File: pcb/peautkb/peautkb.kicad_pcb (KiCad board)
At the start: 4 copper layers, 3.6 x 3.1 mm, 184 parts, among them J1 Conn_01x04, J2 MJ-4PP-9, J3 Conn_01x04, J4 MJ-4PP-9, SW1 SW_PUSH, SW10 SW_PUSH, SW11 SW_PUSH, SW12 SW_PUSH, SW13 SW_PUSH, SW14 SW_PUSH, SW15 SW_PUSH, SW16 SW_PUSH, SW17 SW_PUSH, SW18 SW_PUSH, SW19 SW_PUSH, SW2 SW_PUSH, SW20 SW_PUSH, SW21 SW_PUSH, SW22 SW_PUSH, SW23 SW_PUSH, SW24 SW_PUSH, SW25 SW_PUSH, SW26 SW_PUSH, SW27 SW_PUSH, SW28 Rotary_Encoder_Switch, SW29 SW_PUSH, SW3 SW_PUSH, SW30 SW_PUSH, SW31 SW_PUSH, SW32 SW_PUSH, SW33 SW_PUSH, SW34 SW_PUSH, SW35 SW_PUSH, SW36 SW_PUSH, SW37 SW_PUSH, SW38 SW_PUSH, SW39 SW_PUSH, SW4 SW_PUSH, SW40 SW_PUSH, SW41 SW_PUSH, SW42 SW_PUSH, SW43 SW_PUSH, SW44 SW_PUSH, SW45 SW_PUSH, SW46 SW_PUSH, SW47 SW_PUSH, SW48 SW_PUSH, SW49 SW_PUSH, SW5 SW_PUSH, SW50 SW_PUSH, SW51 SW_PUSH, SW52 SW_PUSH, SW53 SW_PUSH, SW54 SW_PUSH, SW55 SW_PUSH, SW56 SW_PUSH, SW57 Rotary_Encoder_Switch, SW58 SW_PUSH, SW6 SW_PUSH, SW7 SW_PUSH, SW8 SW_PUSH, SW9 SW_PUSH, U1 black-pill-v3, U2 black-pill-v3

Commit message: left side traces completed
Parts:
- removed D2, D3, D36, D37, D38, D4: D, kbd:D3_SMD_v2
- removed SW1, SW2, SW3, SW30, SW31, SW32: SW_PUSH, kbd:CherryMX_Hotswap
- added REF**: Breakaway_Tabs, kbd:Breakaway_Tabs, F.Cu at (17.8, 89.2)
- added REF**: Breakaway_Tabs, kbd:Breakaway_Tabs, F.Cu at (182.0, 80.4)
- added REF**: Breakaway_Tabs, kbd:Breakaway_Tabs, F.Cu at (189.8, 37.2)
- added REF**: Breakaway_Tabs, kbd:Breakaway_Tabs, F.Cu at (182.0, 37.3)
- added REF**: Breakaway_Tabs, kbd:Breakaway_Tabs, F.Cu at (189.7, 80.4)
- added REF**: Breakaway_Tabs, kbd:Breakaway_Tabs, F.Cu at (353.9, 44.9)
- added REF**: Breakaway_Tabs, kbd:Breakaway_Tabs, F.Cu at (353.8, 88.8)
- added REF**: Breakaway_Tabs, kbd:Breakaway_Tabs, F.Cu at (344.2, 97.7)
- added REF**: Breakaway_Tabs, kbd:Breakaway_Tabs, F.Cu at (292.5, 97.7)
- added REF**: Breakaway_Tabs, kbd:Breakaway_Tabs, F.Cu at (17.8, 46.8)
- added REF**: Breakaway_Tabs, kbd:Breakaway_Tabs, F.Cu at (28.3, 97.7)
- added REF**: Breakaway_Tabs, kbd:Breakaway_Tabs, F.Cu at (79.3, 97.7)
- D1, D10, D11, D12, D13, D14, D15, D16, D17, D18, D19, D20, D21, D22, D23, D24, D25, D26, D27, D28, D29, D30, D31, D32, D33, D35, D39, D40, D41, D42, D43, D44, D45, D46, D47, D48, D49, D5, D50, D51, D56, D6, D61, D62, D7, D8, D9, LED1, LED10, LED11, LED12, LED13, LED14, LED15, LED16, LED17, LED18, LED19, LED2, LED20, LED21, LED22, LED23, LED24, LED25, LED26, LED27, LED28, LED29, LED3, LED30, LED31, LED32, LED33, LED34, LED35, LED36, LED37, LED38, LED39, LED4, LED40, LED41, LED42, LED43, LED44, LED45, LED46, LED47, LED48, LED49, LED5, LED50, LED6, LED7, LED8, LED9: moved to B.Cu
- D52, D53, D54, D55, D57, D58, D59, D60, D63, D64, D65, D66, D67, D68, D69, D70: footprint kbd:D3_SMD -> kbd:D3_SMD_v2; moved to B.Cu
- moved LED3 340.6 mm to (27.4, 92.4), turned to 180 degrees
- moved SW4 303.1 mm to (27.4, 50.0)
- moved LED2 299.6 mm to (27.5, 73.5)
- moved SW58 288.1 mm to (210.7, 106.2), turned to 26.7 degrees
- moved SW5 286.9 mm to (27.4, 69.0)
- moved SW42 286.4 mm to (306.2, 69.0)
- moved SW37 282.9 mm to (325.2, 63.3)
- moved SW38 281.8 mm to (325.2, 82.3)
- moved SW35 279.6 mm to (344.1, 88.0)
- moved SW6 271.2 mm to (27.4, 88.0)
- moved D10 266.3 mm to (54.7, 43.4), turned to 90 degrees
- moved LED50 266.1 mm to (212.8, 110.0), turned to 26.7 degrees
- moved SW41 265.3 mm to (287.2, 88.0)
- moved SW45 265.0 mm to (267.4, 89.2), turned to 6.7 degrees
- moved SW53 263.4 mm to (228.9, 98.3), turned to 20 degrees
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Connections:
- D18 pad 2: Net-(D13-Pad4) -> LLED_In
- D22 pad 2: Net-(D18-Pad4) -> Net-(D22-Pad2)
- D46 pad 2: Net-(D42-Pad4) -> RLED_In
- D5 pad 2: Net-(D1-Pad4) -> Net-(D5-Pad2)
- D51 pad 2: Net-(D46-Pad4) -> Net-(D51-Pad2)
- D56 pad 2: Net-(D51-Pad4) -> Net-(D56-Pad2)
- D61 pad 2: Net-(D56-Pad4) -> Net-(D61-Pad2)
- D62 pad 2: Net-(D61-Pad4) -> Net-(D62-Pad2)
- D9 pad 2: Net-(D5-Pad4) -> Net-(D9-Pad2)
- D9 pad 4: Net-(D13-Pad2) -> Net-(D9-Pad4)
- LED11 pad 4: Net-(LED11-Pad4) -> Net-(D9-Pad4)
- LED12 pad 2: Net-(LED11-Pad4) -> Net-(LED12-Pad2)
- LED13 pad 2: Net-(LED12-Pad4) -> Net-(LED13-Pad2)
- LED13 pad 4: Net-(LED13-Pad4) -> Net-(D13-Pad4)
- LED14 pad 2: Net-(LED13-Pad4) -> Net-(LED14-Pad2)
- LED14 pad 4: Net-(LED14-Pad4) -> Net-(LED10-Pad2)
- LED15 pad 2: Net-(LED15-Pad2) -> Net-(D9-Pad2)
- LED16 pad 4: Net-(LED15-Pad2) -> Net-(LED12-Pad2)
- LED17 pad 2: Net-(LED17-Pad2) -> Net-(D13-Pad2)
- LED17 pad 4: Net-(LED16-Pad2) -> Net-(LED17-Pad4)
- LED18 pad 2: Net-(LED14-Pad4) -> Net-(LED18-Pad2)
- LED18 pad 4: Net-(LED17-Pad2) -> Net-(LED14-Pad2)
- LED20 pad 2: Net-(LED19-Pad4) -> Net-(LED20-Pad2)
- LED20 pad 4: Net-(LED20-Pad4) -> Net-(LED16-Pad2)
- LED21 pad 2: Net-(LED20-Pad4) -> Net-(LED17-Pad4)
- LED22 pad 2: Net-(LED21-Pad4) -> Net-(LED22-Pad2)
- LED22 pad 4: Net-(LED22-Pad4) -> Net-(LED18-Pad2)
- LED23 pad 2: Net-(LED23-Pad2) -> Net-(LED19-Pad4)
- LED23 pad 4: LLED_In -> Net-(D18-Pad4)
- LED24 pad 2: Net-(LED24-Pad2) -> Net-(LED21-Pad4)
- LED24 pad 4: Net-(LED23-Pad2) -> Net-(LED20-Pad2)
- LED25 pad 2: Net-(LED22-Pad4) -> Net-(D22-Pad2)
- LED25 pad 4: Net-(LED24-Pad2) -> Net-(LED22-Pad2)
- LED28 pad 2: Net-(D42-Pad2) -> Net-(LED28-Pad2)
- LED28 pad 4: Net-(LED27-Pad2) -> Net-(LED28-Pad4)
- LED29 pad 4: Net-(LED29-Pad4) -> Net-(D51-Pad4)
- LED3 pad 2: Net-(D1-Pad2) -> Net-(LED10-Pad4)
- LED3 pad 4: Net-(LED2-Pad2) -> Net-(LED3-Pad4)
- LED30 pad 2: Net-(LED29-Pad4) -> Net-(LED30-Pad2)
- LED30 pad 4: Net-(LED30-Pad4) -> Net-(LED27-Pad2)
- LED31 pad 2: Net-(LED30-Pad4) -> Net-(LED28-Pad4)
- LED31 pad 4: Net-(LED31-Pad4) -> Net-(D56-Pad4)
- LED32 pad 2: Net-(LED32-Pad2) -> Net-(D51-Pad2)
- LED33 pad 4: Net-(LED32-Pad2) -> Net-(LED30-Pad2)
- LED34 pad 2: Net-(LED34-Pad2) -> Net-(D56-Pad2)
- LED34 pad 4: Net-(LED33-Pad2) -> Net-(LED34-Pad4)
- LED35 pad 2: Net-(LED31-Pad4) -> Net-(LED35-Pad2)
- LED35 pad 4: Net-(LED34-Pad2) -> Net-(LED28-Pad2)
- LED36 pad 4: Net-(LED36-Pad4) -> Net-(D42-Pad4)
- LED37 pad 2: Net-(LED36-Pad4) -> Net-(LED37-Pad2)
- LED37 pad 4: Net-(LED37-Pad4) -> Net-(LED33-Pad2)
- LED38 pad 2: Net-(LED37-Pad4) -> Net-(LED34-Pad4)
- LED38 pad 4: Net-(LED38-Pad4) -> Net-(D61-Pad4)
- LED39 pad 2: Net-(LED38-Pad4) -> Net-(LED39-Pad2)
- LED39 pad 4: Net-(LED39-Pad4) -> Net-(LED35-Pad2)
- LED4 pad 4: Net-(LED4-Pad4) -> Net-(D1-Pad4)
- LED40 pad 2: Net-(LED40-Pad2) -> Net-(D42-Pad2)
- LED41 pad 4: Net-(LED40-Pad2) -> Net-(LED37-Pad2)
- LED42 pad 2: Net-(LED42-Pad2) -> Net-(D61-Pad2)
- LED42 pad 4: Net-(LED41-Pad2) -> Net-(LED42-Pad4)
- LED43 pad 2: Net-(LED39-Pad4) -> Net-(LED43-Pad2)
- LED43 pad 4: Net-(LED42-Pad2) -> Net-(LED39-Pad2)
- LED45 pad 2: Net-(LED44-Pad4) -> Net-(LED45-Pad2)
- LED45 pad 4: Net-(LED45-Pad4) -> Net-(LED41-Pad2)
- LED46 pad 2: Net-(LED45-Pad4) -> Net-(LED42-Pad4)
- LED47 pad 2: Net-(LED46-Pad4) -> Net-(LED47-Pad2)
- LED47 pad 4: Net-(LED47-Pad4) -> Net-(LED43-Pad2)
- LED48 pad 2: Net-(LED48-Pad2) -> Net-(LED44-Pad4)
- LED48 pad 4: RLED_In -> Net-(D46-Pad4)
- LED49 pad 2: Net-(LED49-Pad2) -> Net-(LED46-Pad4)
- LED49 pad 4: Net-(LED48-Pad2) -> Net-(LED45-Pad2)
- LED5 pad 2: Net-(LED4-Pad4) -> Net-(LED5-Pad2)
- LED5 pad 4: Net-(LED5-Pad4) -> Net-(LED2-Pad2)
- LED50 pad 2: Net-(LED47-Pad4) -> Net-(D62-Pad2)
- LED50 pad 4: Net-(LED49-Pad2) -> Net-(LED47-Pad2)
- LED6 pad 2: Net-(LED5-Pad4) -> Net-(LED3-Pad4)
- LED6 pad 4: Net-(LED10-Pad2) -> Net-(D5-Pad4)
- LED7 pad 2: Net-(LED7-Pad2) -> Net-(D1-Pad2)
- LED8 pad 2: Net-(LED8-Pad2) -> Net-(LED12-Pad4)
- LED8 pad 4: Net-(LED7-Pad2) -> Net-(LED5-Pad2)
- LED9 pad 2: Net-(LED10-Pad4) -> Net-(D5-Pad2)
- LED9 pad 4: Net-(LED8-Pad2) -> Net-(LED13-Pad2)
- SW8 pad 1: Net-(SW8-Pad1) -> LCol2
- SW9 pad 1: Net-(SW8-Pad1) -> LCol2
- U1 pad 33: LCol0 -> Net-(U1-Pad33)
- U1 pad 34: LRow0 -> LRow3
- U1 pad 35: LRow1 -> LRow2
- U1 pad 36: LRow2 -> LRow1
- U1 pad 37: LRow3 -> LRow0
- U2 pad 33: RCol0 -> Net-(U2-Pad33)
- U2 pad 34: RRow0 -> RRow3
- U2 pad 35: RRow1 -> RRow2
- U2 pad 36: RRow2 -> RRow1
- U2 pad 37: RRow3 -> RRow0
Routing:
- net LCol1: track 0.00 -> 230.7 mm
- net LCol3: track 0.00 -> 228.8 mm, vias 0 -> 7
- net LCol2: track 0.00 -> 218.8 mm, vias 0 -> 6
- net LCol4: track 0.00 -> 218.1 mm, vias 0 -> 7
- net LCol5: track 0.00 -> 196.7 mm, vias 0 -> 7
- net LRow1: track 0.00 -> 194.5 mm, vias 0 -> 2
- net LRow2: track 0.00 -> 192.3 mm, vias 0 -> 6
- net LRow3: track 0.00 -> 184.7 mm, vias 0 -> 7
- net LCol6: track 0.00 -> 182.3 mm, vias 0 -> 7
- net LRow0: track 0.00 -> 180.0 mm
- net LCol7: track 0.00 -> 166.9 mm, vias 0 -> 4
- net GND1: track 0.00 -> 60.9 mm, vias 0 -> 31
- net Net-(LED10-Pad4): track 0.00 -> 58.6 mm
- net LUSART_RX: track 0.00 -> 57.8 mm, vias 0 -> 1
- net LUSART_TX: track 0.00 -> 55.1 mm
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- added copper zone on In1.Cu, net GND1
- added copper zone on In2.Cu, net VDD
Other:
- board size 3.6 x 3.1 mm -> 348 x 113 mm

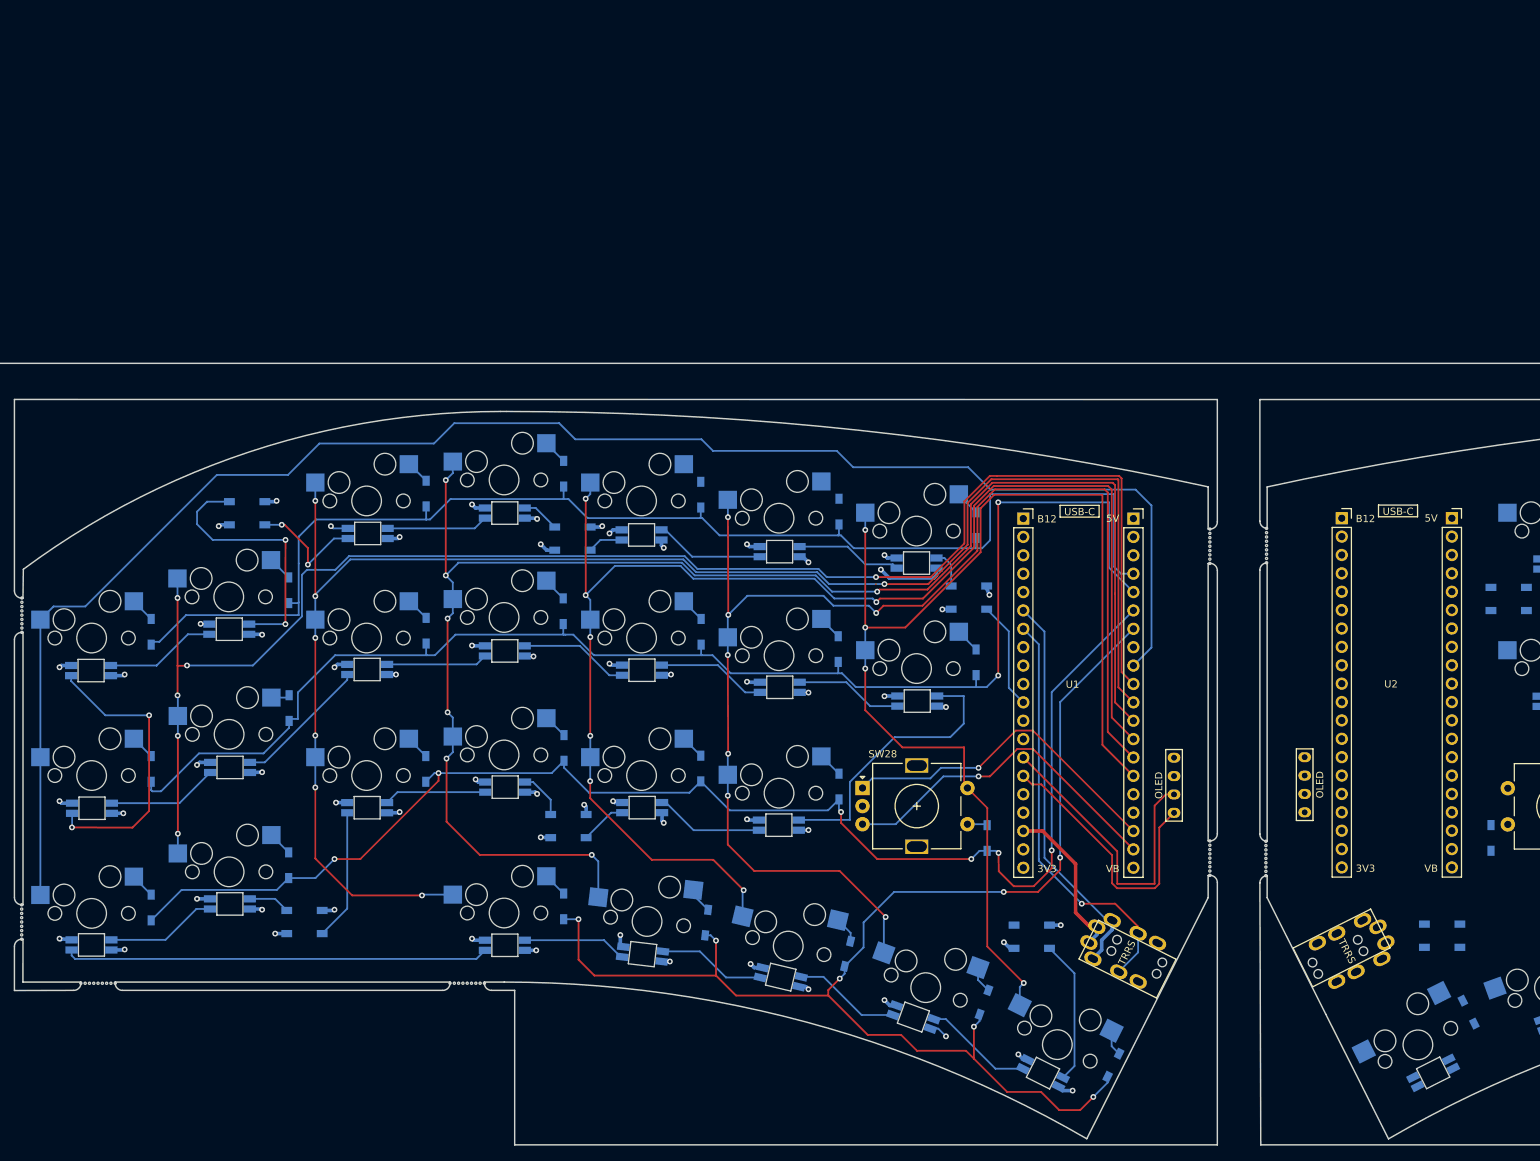
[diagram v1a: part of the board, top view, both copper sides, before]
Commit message: aadded decoup caps to LHS
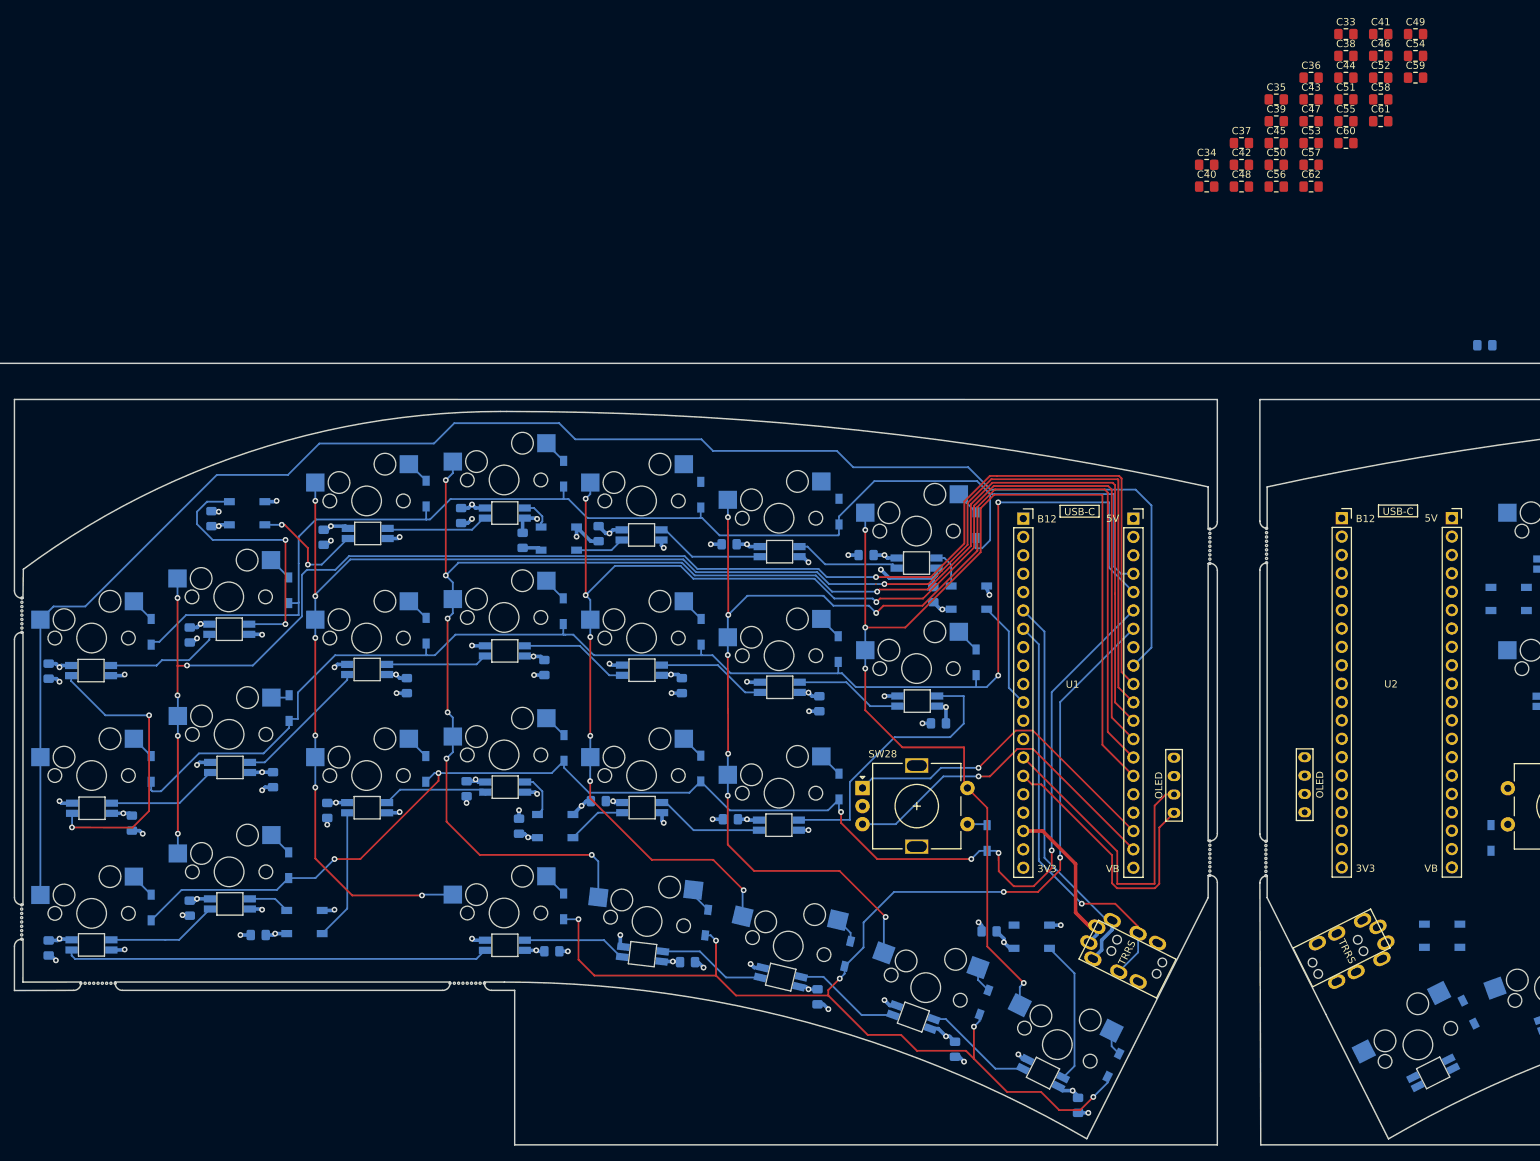
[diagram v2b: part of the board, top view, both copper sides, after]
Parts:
- added C1: 100nF, Capacitor_SMD:C_0805_2012Metric_Pad1.18x1.45mm_HandSolder, B.Cu at (79.2, 70.8)
- added C10: 100nF, Capacitor_SMD:C_0805_2012Metric_Pad1.18x1.45mm_HandSolder, B.Cu at (87.0, 36.5)
- added C11: 100nF, Capacitor_SMD:C_0805_2012Metric_Pad1.18x1.45mm_HandSolder, B.Cu at (127.8, 99.5)
- added C12: 100nF, Capacitor_SMD:C_0805_2012Metric_Pad1.18x1.45mm_HandSolder, B.Cu at (52.5, 69.5)
- added C13: 100nF, Capacitor_SMD:C_0805_2012Metric_Pad1.18x1.45mm_HandSolder, B.Cu at (115.7, 75.0)
- added C14: 100nF, Capacitor_SMD:C_0805_2012Metric_Pad1.18x1.45mm_HandSolder, B.Cu at (97.5, 35.5)
- added C15: 100nF, Capacitor_SMD:C_0805_2012Metric_Pad1.18x1.45mm_HandSolder, B.Cu at (50.5, 91.0)
- added C16: 100nF, Capacitor_SMD:C_0805_2012Metric_Pad1.18x1.45mm_HandSolder, B.Cu at (44.0, 33.5)
- added C17: 100nF, Capacitor_SMD:C_0805_2012Metric_Pad1.18x1.45mm_HandSolder, B.Cu at (163.8, 114.5)
- added C18: 100nF, Capacitor_SMD:C_0805_2012Metric_Pad1.18x1.45mm_HandSolder, B.Cu at (115.5, 37.0)
- added C19: 100nF, Capacitor_SMD:C_0805_2012Metric_Pad1.18x1.45mm_HandSolder, B.Cu at (90.0, 54.0)
- added C2: 100nF, Capacitor_SMD:C_0805_2012Metric_Pad1.18x1.45mm_HandSolder, B.Cu at (144.5, 61.8)
- added C20: 100nF, Capacitor_SMD:C_0805_2012Metric_Pad1.18x1.45mm_HandSolder, B.Cu at (60.0, 73.8)
- added C21: 100nF, Capacitor_SMD:C_0805_2012Metric_Pad1.18x1.45mm_HandSolder, B.Cu at (59.5, 36.0)
- added C22: 100nF, Capacitor_SMD:C_0805_2012Metric_Pad1.18x1.45mm_HandSolder, B.Cu at (146.8, 106.8)
- added C23: 100nF, Capacitor_SMD:C_0805_2012Metric_Pad1.18x1.45mm_HandSolder, B.Cu at (33.0, 75.5)
- added C24: 100nF, Capacitor_SMD:C_0805_2012Metric_Pad1.18x1.45mm_HandSolder, B.Cu at (134.5, 38.5)
- added C25: 100nF, Capacitor_SMD:C_0805_2012Metric_Pad1.18x1.45mm_HandSolder, B.Cu at (151.5, 90.5)
- added C26: 100nF, Capacitor_SMD:C_0805_2012Metric_Pad1.18x1.45mm_HandSolder, B.Cu at (78.5, 33.0)
- added C27: 100nF, Capacitor_SMD:C_0805_2012Metric_Pad1.18x1.45mm_HandSolder, B.Cu at (97.5, 72.5)
- added C28: 100nF, Capacitor_SMD:C_0805_2012Metric_Pad1.18x1.45mm_HandSolder, B.Cu at (109.8, 94.8)
- added C29: 100nF, Capacitor_SMD:C_0805_2012Metric_Pad1.18x1.45mm_HandSolder, B.Cu at (21.5, 54.5)
- added C3: 100nF, Capacitor_SMD:C_0805_2012Metric_Pad1.18x1.45mm_HandSolder, B.Cu at (41.0, 87.3)
- added C30: 100nF, Capacitor_SMD:C_0805_2012Metric_Pad1.18x1.45mm_HandSolder, B.Cu at (143.8, 44.0)
- added C31: 100nF, Capacitor_SMD:C_0805_2012Metric_Pad1.18x1.45mm_HandSolder, B.Cu at (109.0, 56.5)
- added C32: 100nF, Capacitor_SMD:C_0805_2012Metric_Pad1.18x1.45mm_HandSolder, B.Cu at (220.0, 9.50)
- added C33: 100nF, Capacitor_SMD:C_0805_2012Metric_Pad1.18x1.45mm_HandSolder, F.Cu at (200.8, -33.5)
- added C34: 100nF, Capacitor_SMD:C_0805_2012Metric_Pad1.18x1.45mm_HandSolder, F.Cu at (181.5, -15.4)
- added C35: 100nF, Capacitor_SMD:C_0805_2012Metric_Pad1.18x1.45mm_HandSolder, F.Cu at (191.1, -24.5)
- added C36: 100nF, Capacitor_SMD:C_0805_2012Metric_Pad1.18x1.45mm_HandSolder, F.Cu at (196.0, -27.5)
- added C37: 100nF, Capacitor_SMD:C_0805_2012Metric_Pad1.18x1.45mm_HandSolder, F.Cu at (186.3, -18.4)
- added C38: 100nF, Capacitor_SMD:C_0805_2012Metric_Pad1.18x1.45mm_HandSolder, F.Cu at (200.8, -30.5)
- added C39: 100nF, Capacitor_SMD:C_0805_2012Metric_Pad1.18x1.45mm_HandSolder, F.Cu at (191.1, -21.5)
- added C4: 100nF, Capacitor_SMD:C_0805_2012Metric_Pad1.18x1.45mm_HandSolder, B.Cu at (71.0, 56.5)
- added C40: 100nF, Capacitor_SMD:C_0805_2012Metric_Pad1.18x1.45mm_HandSolder, F.Cu at (181.5, -12.4)
- added C41: 100nF, Capacitor_SMD:C_0805_2012Metric_Pad1.18x1.45mm_HandSolder, F.Cu at (205.6, -33.5)
- added C42: 100nF, Capacitor_SMD:C_0805_2012Metric_Pad1.18x1.45mm_HandSolder, F.Cu at (186.3, -15.4)
- added C43: 100nF, Capacitor_SMD:C_0805_2012Metric_Pad1.18x1.45mm_HandSolder, F.Cu at (196.0, -24.5)
- added C44: 100nF, Capacitor_SMD:C_0805_2012Metric_Pad1.18x1.45mm_HandSolder, F.Cu at (200.8, -27.5)
- added C45: 100nF, Capacitor_SMD:C_0805_2012Metric_Pad1.18x1.45mm_HandSolder, F.Cu at (191.1, -18.4)
- added C46: 100nF, Capacitor_SMD:C_0805_2012Metric_Pad1.18x1.45mm_HandSolder, F.Cu at (205.6, -30.5)
- added C47: 100nF, Capacitor_SMD:C_0805_2012Metric_Pad1.18x1.45mm_HandSolder, F.Cu at (196.0, -21.5)
- added C48: 100nF, Capacitor_SMD:C_0805_2012Metric_Pad1.18x1.45mm_HandSolder, F.Cu at (186.3, -12.4)
- added C49: 100nF, Capacitor_SMD:C_0805_2012Metric_Pad1.18x1.45mm_HandSolder, F.Cu at (210.4, -33.5)
- added C5: 100nF, Capacitor_SMD:C_0805_2012Metric_Pad1.18x1.45mm_HandSolder, B.Cu at (86.5, 76.0)
- added C50: 100nF, Capacitor_SMD:C_0805_2012Metric_Pad1.18x1.45mm_HandSolder, F.Cu at (191.1, -15.4)
- added C51: 100nF, Capacitor_SMD:C_0805_2012Metric_Pad1.18x1.45mm_HandSolder, F.Cu at (200.8, -24.5)
- added C52: 100nF, Capacitor_SMD:C_0805_2012Metric_Pad1.18x1.45mm_HandSolder, F.Cu at (205.6, -27.5)
- added C53: 100nF, Capacitor_SMD:C_0805_2012Metric_Pad1.18x1.45mm_HandSolder, F.Cu at (196.0, -18.4)
- added C54: 100nF, Capacitor_SMD:C_0805_2012Metric_Pad1.18x1.45mm_HandSolder, F.Cu at (210.4, -30.5)
- added C55: 100nF, Capacitor_SMD:C_0805_2012Metric_Pad1.18x1.45mm_HandSolder, F.Cu at (200.8, -21.5)
- added C56: 100nF, Capacitor_SMD:C_0805_2012Metric_Pad1.18x1.45mm_HandSolder, F.Cu at (191.1, -12.4)
- added C57: 100nF, Capacitor_SMD:C_0805_2012Metric_Pad1.18x1.45mm_HandSolder, F.Cu at (196.0, -15.4)
- added C58: 100nF, Capacitor_SMD:C_0805_2012Metric_Pad1.18x1.45mm_HandSolder, F.Cu at (205.6, -24.5)
- added C59: 100nF, Capacitor_SMD:C_0805_2012Metric_Pad1.18x1.45mm_HandSolder, F.Cu at (210.4, -27.5)
- added C6: 100nF, Capacitor_SMD:C_0805_2012Metric_Pad1.18x1.45mm_HandSolder, B.Cu at (91.0, 93.2)
- added C60: 100nF, Capacitor_SMD:C_0805_2012Metric_Pad1.18x1.45mm_HandSolder, F.Cu at (200.8, -18.4)
- added C61: 100nF, Capacitor_SMD:C_0805_2012Metric_Pad1.18x1.45mm_HandSolder, F.Cu at (205.6, -21.5)
- added C62: 100nF, Capacitor_SMD:C_0805_2012Metric_Pad1.18x1.45mm_HandSolder, F.Cu at (196.0, -12.4)
- added C7: 100nF, Capacitor_SMD:C_0805_2012Metric_Pad1.18x1.45mm_HandSolder, B.Cu at (41.0, 49.5)
- added C8: 100nF, Capacitor_SMD:C_0805_2012Metric_Pad1.18x1.45mm_HandSolder, B.Cu at (128.0, 59.0)
- added C9: 100nF, Capacitor_SMD:C_0805_2012Metric_Pad1.18x1.45mm_HandSolder, B.Cu at (21.5, 92.8)
- moved D9 1.88 mm to (92.0, 36.2)
- moved D13 1.82 mm to (91.5, 75.9)
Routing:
- net GND1: track 60.9 -> 106.8 mm, vias 31 -> 58
- net VDD: track 52.3 -> 96.4 mm, vias 31 -> 30
- net LRow0: track 180.0 -> 185.0 mm
- net Net-(D9-Pad2): track 4.93 -> 6.82 mm
- net Net-(D13-Pad2): track 6.42 -> 8.25 mm
- net Net-(D9-Pad4): track 5.24 -> 4.46 mm
- net Net-(LED13-Pad2): track 14.2 -> 14.9 mm

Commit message: finished RHS
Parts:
- C33, C34, C35, C36, C37, C38, C39, C40, C41, C42, C43, C44, C45, C46, C47, C48, C49, C50, C51, C52, C53, C54, C55, C56, C57, C58, C59, C60, C61, C62: moved to B.Cu
- moved C42 175.9 mm to (346.2, 58.0), turned to 180 degrees
- moved C47 169.9 mm to (338.0, 71.8), turned to 180 degrees
- moved C58 168.8 mm to (330.8, 88.7), turned to 270 degrees
- moved C37 160.8 mm to (331.4, 50.8), turned to 270 degrees
- moved C32 154.9 mm to (350.3, 93.2), turned to 0 degrees
- moved C33 154.1 mm to (308.4, 76.8), turned to 180 degrees
- moved C59 152.6 mm to (315.0, 83.7), turned to 90 degrees
- moved C49 149.0 mm to (319.4, 68.0), turned to 270 degrees
- moved C50 143.3 mm to (326.4, 31.8), turned to 270 degrees
- moved C54 141.6 mm to (279.8, 93.0), turned to 180 degrees
- moved C44 140.6 mm to (207.6, 112.9), turned to 296.7 degrees
- moved C41 136.4 mm to (289.0, 74.4), turned to 180 degrees
- moved C52 133.8 mm to (260.6, 94.5), turned to 180 degrees
- moved C51 131.8 mm to (223.2, 105.4), turned to 180 degrees
- moved C45 130.1 mm to (299.4, 53.8), turned to 180 degrees
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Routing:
- net RCol1: track 0.00 -> 177.8 mm, vias 0 -> 5
- net RRow2: track 0.00 -> 171.8 mm, vias 0 -> 1
- net RCol3: track 0.00 -> 155.8 mm, vias 0 -> 6
- net RRow1: track 0.00 -> 154.8 mm
- net RRow0: track 0.00 -> 152.8 mm
- net RCol2: track 0.00 -> 152.7 mm, vias 0 -> 6
- net RRow3: track 0.00 -> 142.8 mm, vias 0 -> 1
- net RCol4: track 0.00 -> 138.6 mm, vias 0 -> 6
- net RCol5: track 0.00 -> 117.9 mm, vias 0 -> 6
- net GND2: track 0.00 -> 108.3 mm, vias 0 -> 59
- net RCol6: track 0.00 -> 105.0 mm, vias 0 -> 4
- net VCC: track 0.00 -> 101.2 mm, vias 0 -> 31
- net RCol7: track 0.00 -> 95.1 mm, vias 0 -> 4
- net Net-(LED28-Pad2): track 0.00 -> 59.0 mm, vias 0 -> 2
- net RUSART_RX: track 0.00 -> 53.7 mm
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- added copper zone on In1.Cu, net GND2
- added copper zone on In2.Cu, net VCC
